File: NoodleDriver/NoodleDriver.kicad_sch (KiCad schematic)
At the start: 17 parts, among them J1 Conn_01x12, J2 Conn_01x12, U1 WS2811, U2 WS2811, U3 ULN2001, U4 74HC04

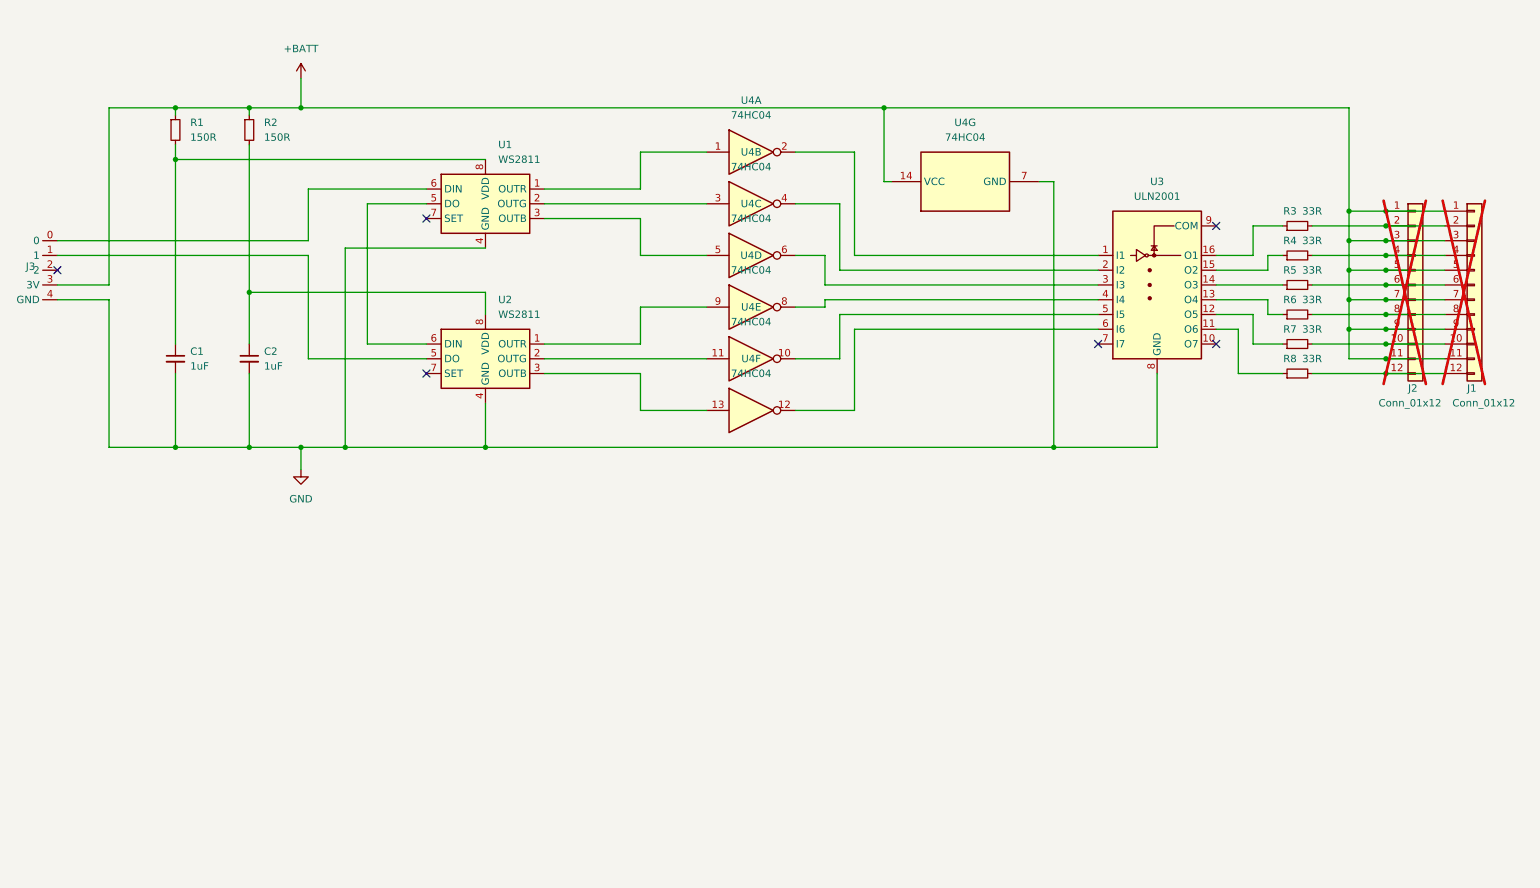
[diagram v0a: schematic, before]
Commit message: Add a microcontroller, and regulator and USB-C connector.  Checkin before I try swapping out the microbit and 0.1" headers.  Part of #8
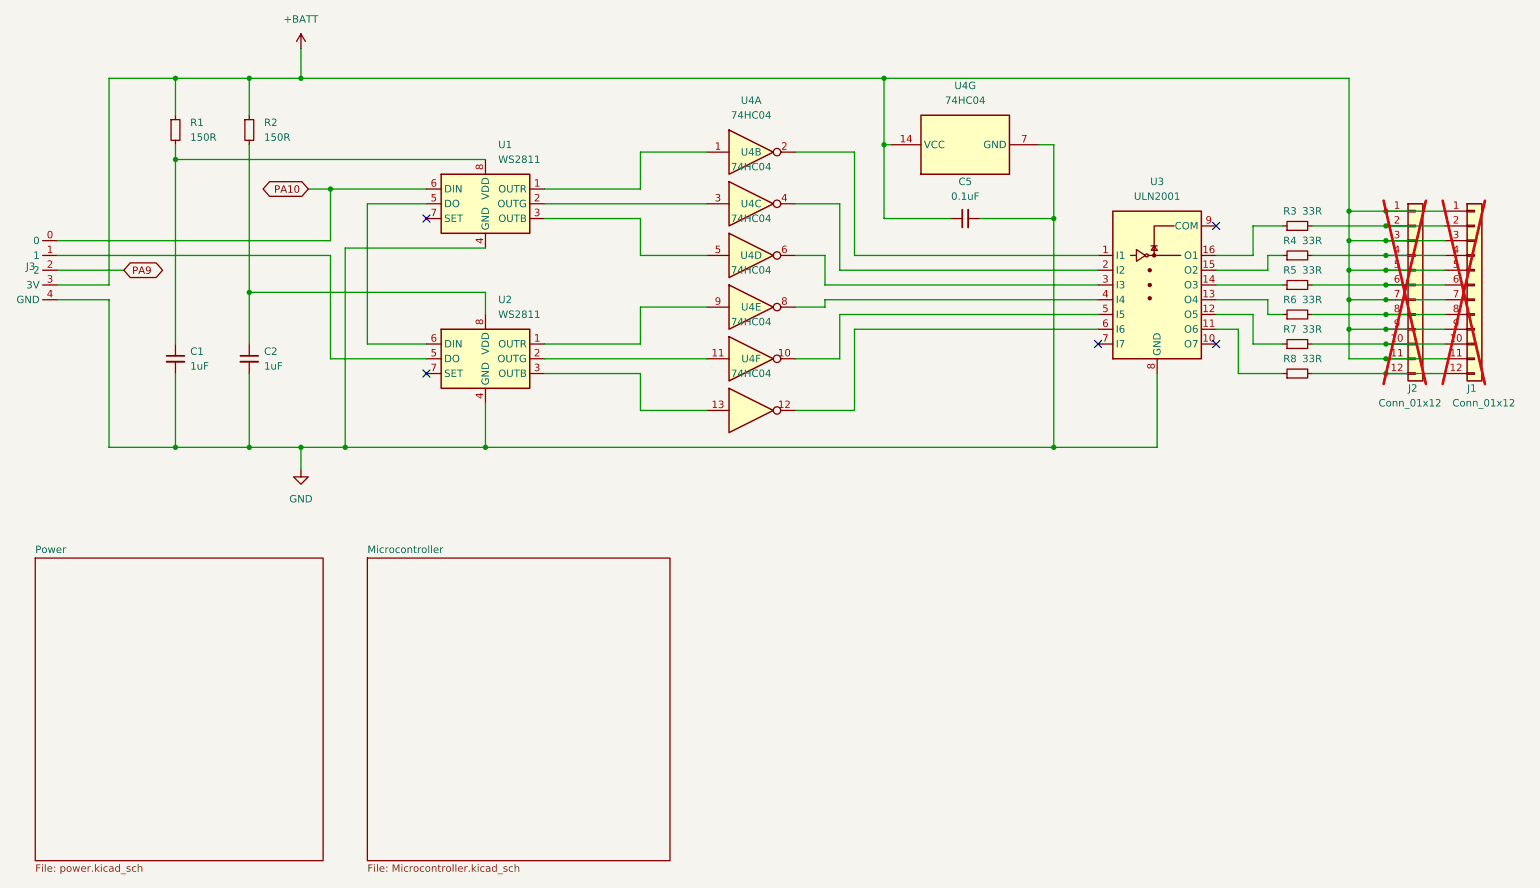
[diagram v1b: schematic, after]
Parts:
- added C5: 0.1uF, Capacitor_SMD:C_0402_1005Metric, symbol Device:C_Small
- C1, C2: footprint (none) -> Capacitor_SMD:C_0402_1005Metric; LCSC (none) -> C14445
- R1, R2: LCSC (none) -> C138054
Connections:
- net +BATT: now also C5.1
- net GND: now also C5.2
- net PA10: now reaches J3.0, U1.6 (DIN)
- net PA9: now reaches J3.2
- no-connect marks 6 -> 5
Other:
- added sheet Microcontroller (Microcontroller.kicad_sch)
- added sheet Power (power.kicad_sch)
- moved on the sheet: U4G

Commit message: Final tuning of prototype board, which we've ordered a handful of prototypes to be fabbed.  Part of #8
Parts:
- removed J1: Conn_01x12, Connector-1x12-horizontal-smd:Connector-1x12-horizontal-smd, symbol Connector_Generic:Conn_01x12
- removed J2: Conn_01x12, Connector_PinHeader_2.54mm:PinHeader_1x12_P2.54mm_Vertical, symbol Connector_Generic:Conn_01x12
- removed J3: ~, Microbit-BoltConnector:Microbit Bolt Connector, symbol Microbit-BoltConnector:Microbit_Bolt_Connector
- added J1, J2, J6: Conn_01x04, MagneticPogoPinConnector:MagneticPogoPinConnector_1x04_P2.54mm_Horizontal, symbol Connector_Generic:Conn_01x04
- added J7: Conn_01x04, Connector_PinSocket_2.54mm:PinSocket_1x04_P2.54mm_Vertical, symbol Connector_Generic:Conn_01x04
- added J8: Conn_01x08, Connector_PinSocket_2.54mm:PinSocket_1x08_P2.54mm_Vertical, symbol Connector_Generic:Conn_01x08
- added R17: 1M, Resistor_SMD:R_0402_1005Metric, symbol Device:R_Small
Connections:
- net +BATT: now also J1.1 (Pin_1), J2.1 (Pin_1)
- net GND: now also J8.8 (Pin_8), R17.2
- net at R4.2: now also J1.3 (Pin_3)
- net at R7.2: now also J2.3 (Pin_3)
- net at R8.2: now also J2.4 (Pin_4)
- net at R3.2: now also J1.2 (Pin_2)
- net at R5.2: now also J1.4 (Pin_4)
- net at R6.2: now also J2.2 (Pin_2)
- new net: J6.1 (Pin_1), J7.1 (Pin_1)
- new net: J6.2 (Pin_2), J7.2 (Pin_2)
- new net: J6.3 (Pin_3), J7.3 (Pin_3)
- new net: J6.4 (Pin_4), J7.4 (Pin_4)
- new net +3V3: J8.7 (Pin_7)
- new net PA0: J8.5 (Pin_5)
- new net PA5: J8.4 (Pin_4)
- new net PA6: J8.6 (Pin_6)
- new net PA7: J8.3 (Pin_3)
- new net PB1: R17.1
- new net PB10: J8.2 (Pin_2)
- new net PB11: J8.1 (Pin_1)
